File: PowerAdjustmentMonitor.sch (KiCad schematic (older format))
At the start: 0 parts

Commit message: Added power conditioning outline
did not add current sensing circuit
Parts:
- added JP? (x3): JUMPER, ~, symbol JUMPER
- added R? (x6): R, ~, symbol R
- added R? (x2): RVAR, ~, symbol RVAR
- added U? (x2): LM317H, TO-39, symbol LM317H
- added U? (x2): 7805, symbol 7805
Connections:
- new net: R?.1, R?.2, U?.2 (ADJ)
- new net: R?.2, R?.2, U?.2 (ADJ)
- new net +12V: JP?.1, U?.1 (IN), U?.VI
- new net -12V: JP?.2, U?.1 (IN), U?.VI
- new net AGND: JP?.2, R?.1, R?.1, R?.1, R?.2, U?.GND, U?.GND
- new net FE_V+: JP?.2, U?.VO
- new net V+_ADJ: R?.1, R?.1, U?.3 (OUT)
- new net V+_ADJ_MON: R?.1, R?.2
- new net V-: JP?.1, U?.VO
- new net V-_ADJ: R?.2, R?.2, U?.3 (OUT)
- new net V-_ADJ_MON: R?.1, R?.2

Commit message: Added missing bit
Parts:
- added R? (x2): R, ~, symbol R
- added U? (x2): LM324, symbol LM324
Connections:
- net labels added: V+_MON, V-_MON
- wire segments 53 -> 75
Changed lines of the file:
@@
 Sheet 9 9
 Title ""
-Date "3 feb 2014"
+Date "4 feb 2014"
 Rev ""
 Comp ""
@@
 Text HLabel 5500 6700 2    60   Output ~ 0
 V-_ADJ
-Text HLabel 8000 3300 2    60   Output ~ 0
+Text HLabel 8550 1950 2    60   Output ~ 0
 3V3_MON
-Text HLabel 8000 3450 2    60   Output ~ 0
+Text HLabel 8550 2100 2    60   Output ~ 0
 5V_MON
 Text HLabel 6550 2600 2    60   Output ~ 0
@@
 Text HLabel 6550 5200 2    60   Output ~ 0
 V-_ADJ_MON
-Text HLabel 8000 3900 2    60   Output ~ 0
+Text HLabel 8550 2550 2    60   Output ~ 0
 V+_CURR_MON
-Text HLabel 8000 4050 2    60   Output ~ 0
+Text HLabel 8550 2700 2    60   Output ~ 0
 V-_CURR_MON
 $Comp
@@
 Connection ~ 4050 6000
 Wire Wire Line
-	4050 6700 5500 6700
-Wire Wire Line
 	3850 1200 3850 1350
 Wire Wire Line
@@
 	3450 1900 3450 1500
 Connection ~ 3850 1900
-Wire Wire Line
-	3850 1200 5400 1200
 Wire Wire Line
 	3100 1200 3050 1200
@@
 L +3.3V #PWR?
 U 1 1 52F00C77
-P 7800 3100
-F 0 "#PWR?" H 7800 3060 30  0001 C CNN
-F 1 "+3.3V" H 7800 3210 30  0000 C CNN
-F 2 "" H 7800 3100 60  0000 C CNN
-F 3 "" H 7800 3100 60  0000 C CNN
-	1    7800 3100
+P 8350 1750
+F 0 "#PWR?" H 8350 1710 30  0001 C CNN
+F 1 "+3.3V" H 8350 1860 30  0000 C CNN
+F 2 "" H 8350 1750 60  0000 C CNN
+F 3 "" H 8350 1750 60  0000 C CNN
+	1    8350 1750
 	1    0    0    -1
 $EndComp
@@
 L +5V #PWR?
 U 1 1 52F00C86
-P 7550 3100
-F 0 "#PWR?" H 7550 3190 20  0001 C CNN
-F 1 "+5V" H 7550 3190 30  0000 C CNN
-F 2 "" H 7550 3100 60  0000 C CNN
-F 3 "" H 7550 3100 60  0000 C CNN
-	1    7550 3100
-	1    0    0    -1
-$EndComp
-Wire Wire Line
-	7550 3100 7550 3450
-Wire Wire Line
-	7550 3450 8000 3450
-Wire Wire Line
-	7800 3100 7800 3300
-Wire Wire Line
-	7800 3300 8000 3300
+P 8100 1750
+F 0 "#PWR?" H 8100 1840 20  0001 C CNN
+F 1 "+5V" H 8100 1840 30  0000 C CNN
+F 2 "" H 8100 1750 60  0000 C CNN
+F 3 "" H 8100 1750 60  0000 C CNN
+	1    8100 1750
+	1    0    0    -1
+$EndComp
+Wire Wire Line
+	8100 1750 8100 2100
+Wire Wire Line
+	8100 2100 8550 2100
+Wire Wire Line
+	8350 1750 8350 1950
+Wire Wire Line
+	8350 1950 8550 1950
 $Comp
 L RVAR R?
@@
 	1    0    0    -1
 $EndComp
+Wire Wire Line
+	2150 3950 2150 4200
+$Comp
+L R R?
+U 1 1 52F0BD17
+P 4600 6700
+F 0 "R?" V 4680 6700 40  0000 C CNN
+F 1 "R" V 4607 6701 40  0000 C CNN
+F 2 "~" V 4530 6700 30  0000 C CNN
+F 3 "~" H 4600 6700 30  0000 C CNN
+	1    4600 6700
+	0    -1   -1   0
+$EndComp
+Wire Wire Line
+	4050 6700 4350 6700
+Wire Wire Line
+	4850 6700 5500 6700
+Wire Wire Line
+	4250 6700 4250 6050
+Wire Wire Line
+	4250 6050 4900 6050
+Connection ~ 4250 6700
+Text Label 4500 6050 0    60   ~ 0
+V-_MON
+$Comp
+L R R?
+U 1 1 52F0BE4B
+P 4550 1200
+F 0 "R?" V 4630 1200 40  0000 C CNN
+F 1 "R" V 4557 1201 40  0000 C CNN
+F 2 "~" V 4480 1200 30  0000 C CNN
+F 3 "~" H 4550 1200 30  0000 C CNN
+	1    4550 1200
+	0    -1   -1   0
+$EndComp
+Wire Wire Line
+	4800 1200 5400 1200
+Wire Wire Line
+	4300 1200 3850 1200
+Wire Wire Line
+	4100 1200 4100 1750
+Wire Wire Line
+	4100 1750 4750 1750
+Wire Wire Line
+	4750 1750 4750 1700
+Connection ~ 4100 1200
+Text Label 4300 1750 0    60   ~ 0
+V+_MON
+$Comp
+L LM324 U?
+U 1 1 52F0BFD8
+P 8750 4200
+F 0 "U?" H 8800 4400 60  0000 C CNN
+F 1 "LM324" H 8900 4000 50  0000 C CNN
+F 2 "" H 8750 4200 60  0000 C CNN
+F 3 "" H 8750 4200 60  0000 C CNN
+	1    8750 4200
+	1    0    0    -1
+$EndComp
+$Comp
+L +12V #PWR?
+U 1 1 52F0BFF6
+P 8650 3650
+F 0 "#PWR?" H 8650 3600 20  0001 C CNN
+F 1 "+12V" H 8650 3750 30  0000 C CNN
+F 2 "" H 8650 3650 60  0000 C CNN
+F 3 "" H 8650 3650 60  0000 C CNN
+	1    8650 3650
+	1    0    0    -1
+$EndComp
+$Comp
+L -12V #PWR?
+U 1 1 52F0C005
+P 8650 4750
+F 0 "#PWR?" H 8650 4880 20  0001 C CNN
+F 1 "-12V" H 8650 4850 30  0000 C CNN
+F 2 "" H 8650 4750 60  0000 C CNN
+F 3 "" H 8650 4750 60  0000 C CNN
+	1    8650 4750
+	-1   0    0    1
+$EndComp
+Wire Wire Line
+	8250 4300 8000 4300
+Wire Wire Line
+	8000 4300 8000 4950
+Wire Wire Line
+	8000 4950 9250 4950
+Wire Wire Line
+	9250 4950 9250 4200
+Wire Wire Line
+	8650 4600 8650 4750
+Wire Wire Line
+	8650 3800 8650 3650
+Wire Wire Line
+	8250 4100 7650 4100
+Text Label 7700 4100 0    60   ~ 0
+V+_MON
+$Comp
+L LM324 U?
+U 1 1 52F0C1B4
+P 8850 5950
+F 0 "U?" H 8900 6150 60  0000 C CNN
+F 1 "LM324" H 9000 5750 50  0000 C CNN
+F 2 "" H 8850 5950 60  0000 C CNN
+F 3 "" H 8850 5950 60  0000 C CNN
+	1    8850 5950
+	1    0    0    -1
+$EndComp
+$Comp
+L +12V #PWR?
+U 1 1 52F0C1BA
+P 8750 5400
+F 0 "#PWR?" H 8750 5350 20  0001 C CNN
+F 1 "+12V" H 8750 5500 30  0000 C CNN
+F 2 "" H 8750 5400 60  0000 C CNN
+F 3 "" H 8750 5400 60  0000 C CNN
+	1    8750 5400
+	1    0    0    -1
+$EndComp
+$Comp
+L -12V #PWR?
+U 1 1 52F0C1C0
+P 8750 6500
+F 0 "#PWR?" H 8750 6630 20  0001 C CNN
+F 1 "-12V" H 8750 6600 30  0000 C CNN
+F 2 "" H 8750 6500 60  0000 C CNN
+F 3 "" H 8750 6500 60  0000 C CNN
+	1    8750 6500
+	-1   0    0    1
+$EndComp
+Wire Wire Line
+	8350 6050 8100 6050
+Wire Wire Line
+	8100 6050 8100 6700
+Wire Wire Line
+	8100 6700 9350 6700
+Wire Wire Line
+	9350 6700 9350 5950
+Wire Wire Line
+	8750 6350 8750 6500
+Wire Wire Line
+	8750 5550 8750 5400
+Wire Wire Line
+	8350 5850 7750 5850
+Text Label 7800 5850 0    60   ~ 0
+V-_MON
 $EndSCHEMATC

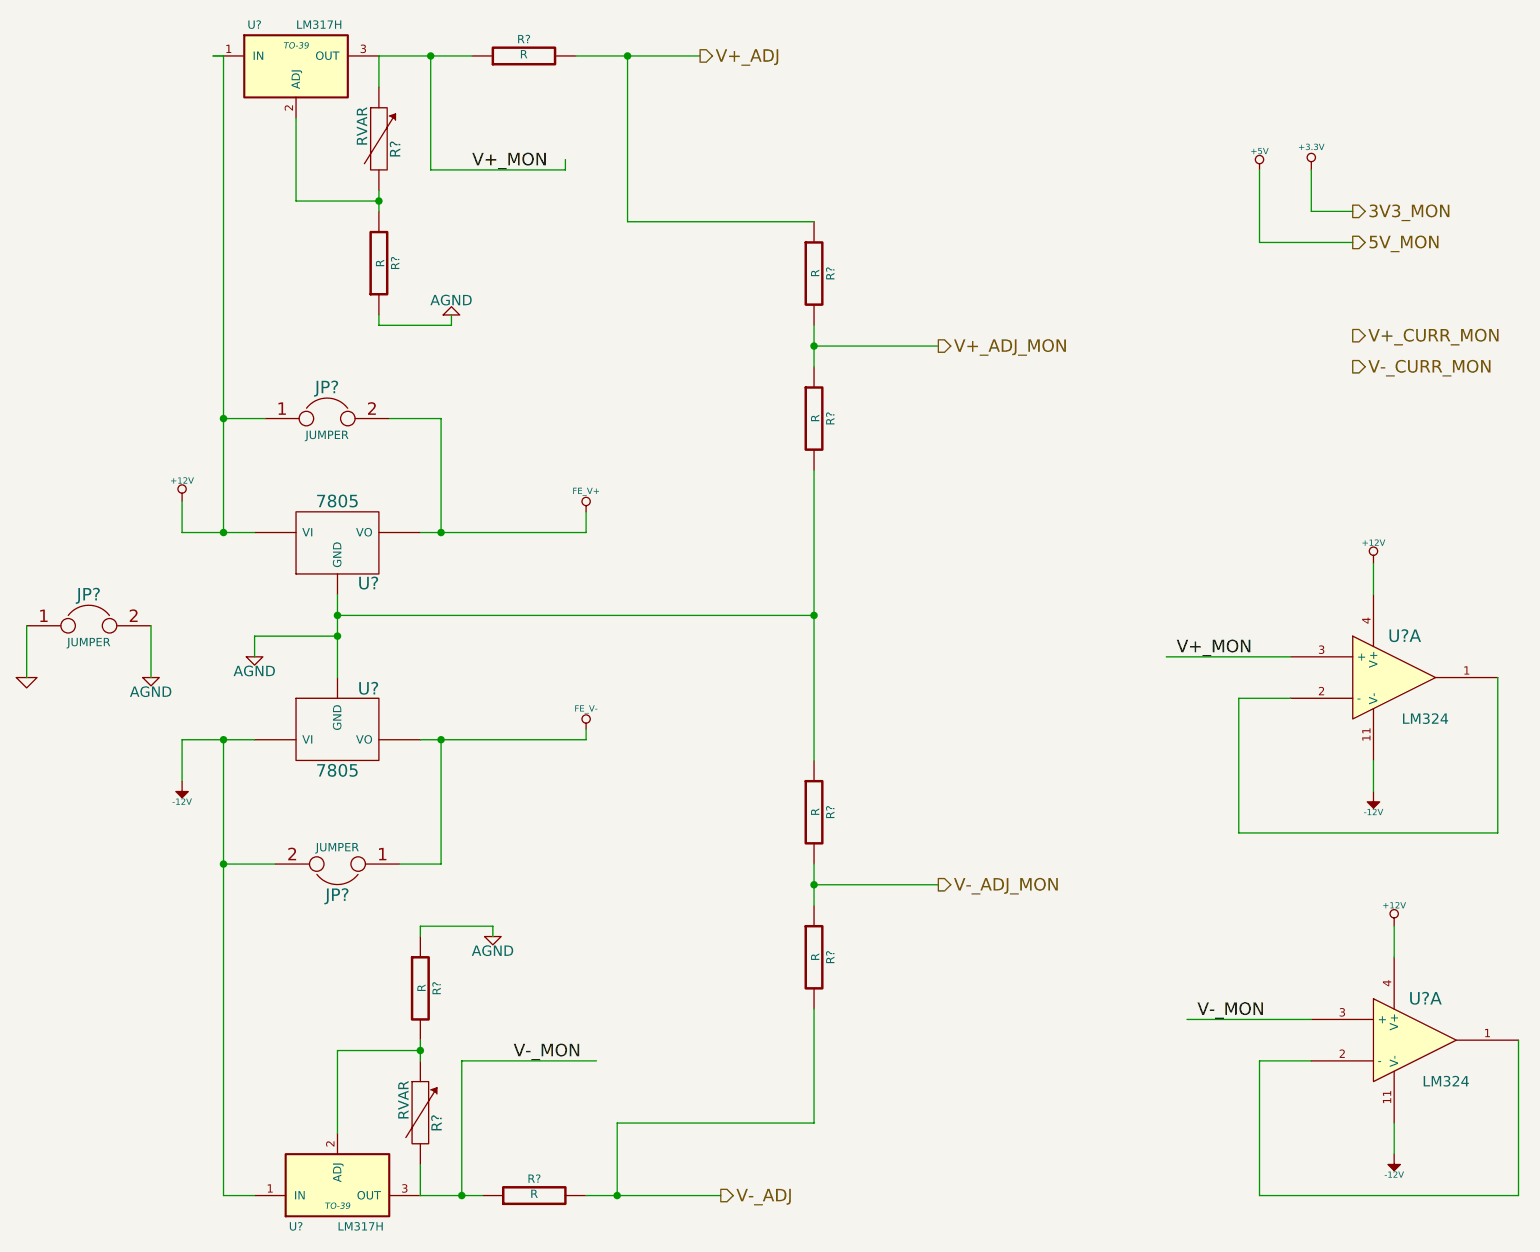
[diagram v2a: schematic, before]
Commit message: Begin Associating relay Module
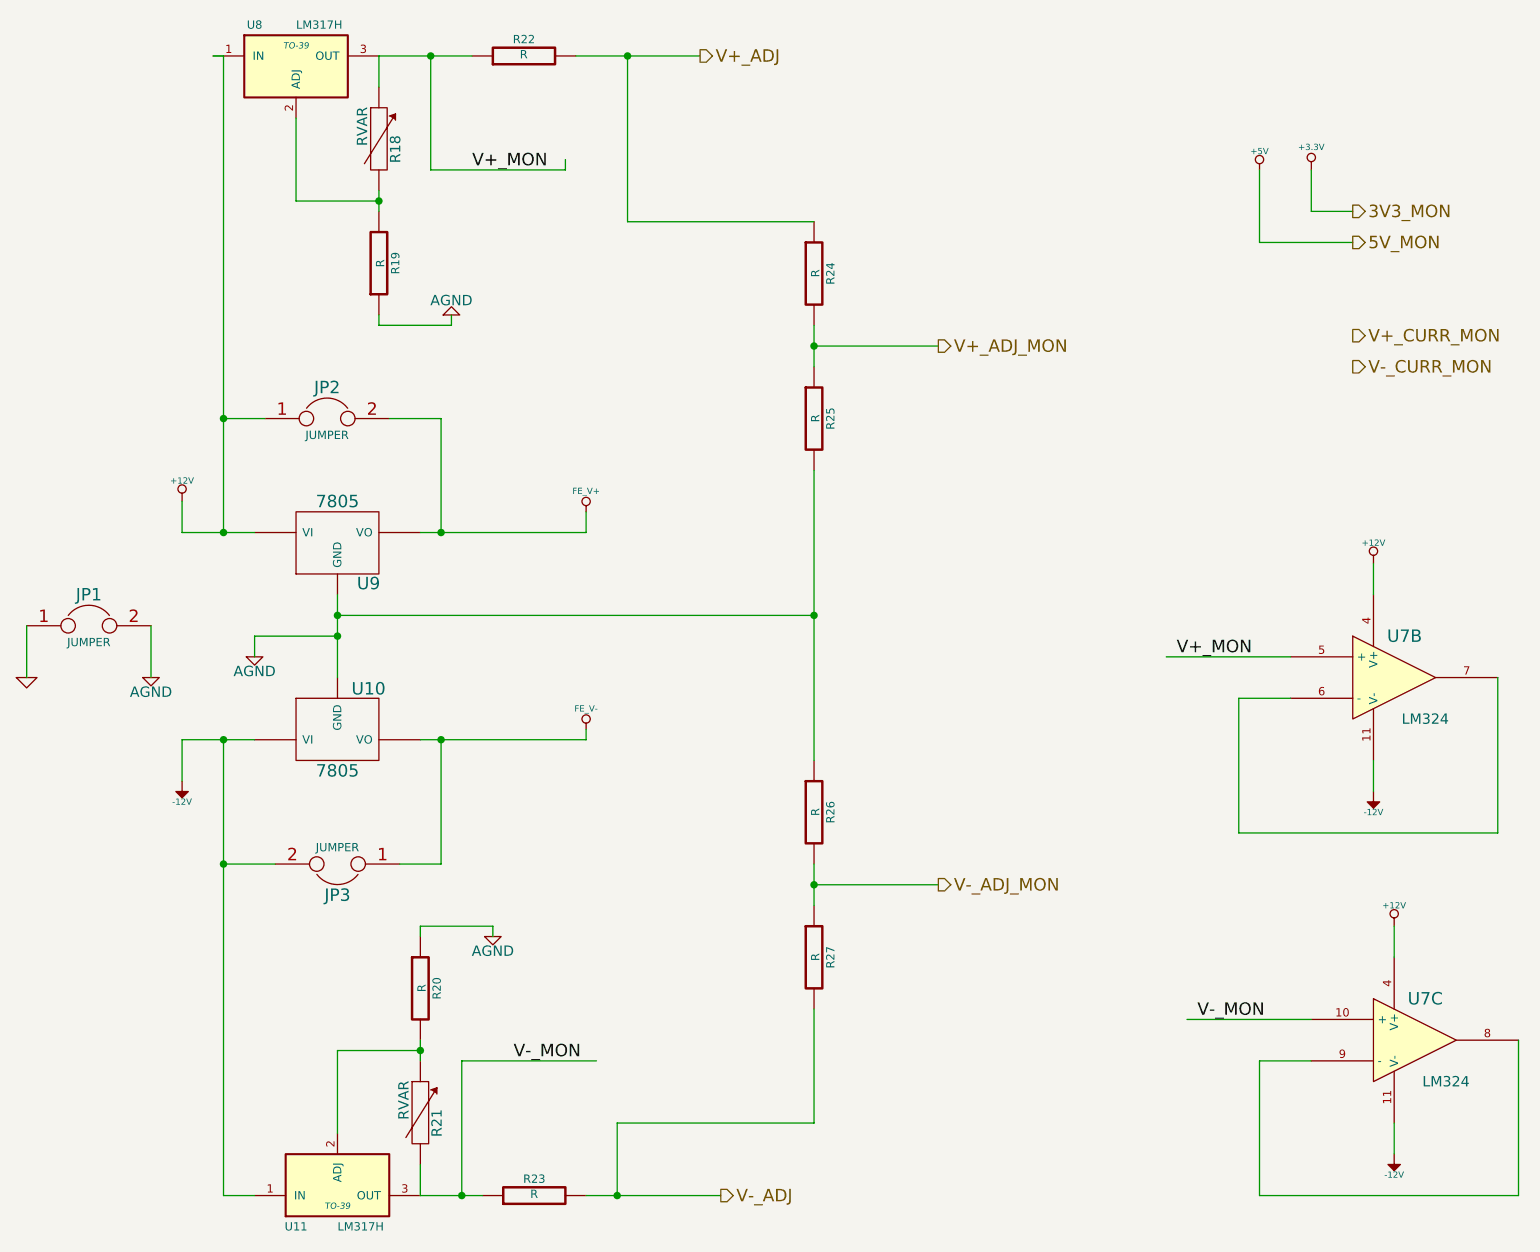
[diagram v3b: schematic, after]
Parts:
- gave numbers to parts that had none: 18
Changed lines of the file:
@@
 LIBS:BenchBudEE
 LIBS:BenchBudEE-cache
-EELAYER 27 0
+EELAYER 24 0
 EELAYER END
 $Descr A4 11693 8268
@@
 $EndDescr
 $Comp
-L +12V #PWR?
+L +12V #PWR41
 U 1 1 52EFE385
 P 2900 3350
-F 0 "#PWR?" H 2900 3300 20  0001 C CNN
+F 0 "#PWR41" H 2900 3300 20  0001 C CNN
 F 1 "+12V" H 2900 3450 30  0000 C CNN
 F 2 "" H 2900 3350 60  0000 C CNN
@@
 $EndComp
 $Comp
-L -12V #PWR?
+L -12V #PWR42
 U 1 1 52EFE394
 P 2900 4700
-F 0 "#PWR?" H 2900 4830 20  0001 C CNN
+F 0 "#PWR42" H 2900 4830 20  0001 C CNN
 F 1 "-12V" H 2900 4800 30  0000 C CNN
 F 2 "" H 2900 4700 60  0000 C CNN
@@
 $EndComp
 $Comp
-L LM317H U?
+L LM317H U11
 U 1 1 52EFE610
 P 3650 6650
-F 0 "U?" H 3450 6850 40  0000 C CNN
+F 0 "U11" H 3450 6850 40  0000 C CNN
 F 1 "LM317H" H 3650 6850 40  0000 L CNN
 F 2 "TO-39" H 3650 6750 30  0000 C CIN
@@
 $EndComp
 $Comp
-L JUMPER JP?
+L JUMPER JP2
 U 1 1 52EFF15A
 P 3600 2950
-F 0 "JP?" H 3600 3100 60  0000 C CNN
+F 0 "JP2" H 3600 3100 60  0000 C CNN
 F 1 "JUMPER" H 3600 2870 40  0000 C CNN
 F 2 "~" H 3600 2950 60  0000 C CNN
@@
 $EndComp
 $Comp
-L JUMPER JP?
+L JUMPER JP3
 U 1 1 52EFF167
 P 3650 5100
-F 0 "JP?" H 3650 5250 60  0000 C CNN
+F 0 "JP3" H 3650 5250 60  0000 C CNN
 F 1 "JUMPER" H 3650 5020 40  0000 C CNN
 F 2 "~" H 3650 5100 60  0000 C CNN
@@
 $EndComp
 $Comp
-L GND #PWR?
+L GND #PWR39
 U 1 1 52EFF203
 P 2150 4200
-F 0 "#PWR?" H 2150 4200 30  0001 C CNN
+F 0 "#PWR39" H 2150 4200 30  0001 C CNN
 F 1 "GND" H 2150 4130 30  0001 C CNN
 F 2 "" H 2150 4200 60  0000 C CNN
@@
 $EndComp
 $Comp
-L AGND #PWR?
+L AGND #PWR40
 U 1 1 52EFF226
 P 2750 4200
-F 0 "#PWR?" H 2750 4200 40  0001 C CNN
+F 0 "#PWR40" H 2750 4200 40  0001 C CNN
 F 1 "AGND" H 2750 4130 50  0000 C CNN
 F 2 "" H 2750 4200 60  0000 C CNN
@@
 $EndComp
 $Comp
-L AGND #PWR?
+L AGND #PWR43
 U 1 1 52EFF247
 P 3250 4100
-F 0 "#PWR?" H 3250 4100 40  0001 C CNN
+F 0 "#PWR43" H 3250 4100 40  0001 C CNN
 F 1 "AGND" H 3250 4030 50  0000 C CNN
 F 2 "" H 3250 4100 60  0000 C CNN
@@
 $EndComp
 $Comp
-L JUMPER JP?
+L JUMPER JP1
 U 1 1 52EFF262
 P 2450 3950
-F 0 "JP?" H 2450 4100 60  0000 C CNN
+F 0 "JP1" H 2450 4100 60  0000 C CNN
 F 1 "JUMPER" H 2450 3870 40  0000 C CNN
 F 2 "~" H 2450 3950 60  0000 C CNN
@@
 $EndComp
 $Comp
-L FE_V+ #PWR?
+L FE_V+ #PWR46
 U 1 1 52EFF50B
 P 4850 3400
-F 0 "#PWR?" H 4850 3500 30  0001 C CNN
+F 0 "#PWR46" H 4850 3500 30  0001 C CNN
 F 1 "FE_V+" H 4850 3500 30  0000 C CNN
 F 2 "" H 4850 3400 60  0000 C CNN
@@
 $EndComp
 $Comp
-L FE_V- #PWR?
+L FE_V- #PWR47
 U 1 1 52EFF51A
 P 4850 4450
-F 0 "#PWR?" H 4850 4550 30  0001 C CNN
+F 0 "#PWR47" H 4850 4550 30  0001 C CNN
 F 1 "FE_V-" H 4850 4550 30  0000 C CNN
 F 2 "" H 4850 4450 60  0000 C CNN
@@
 $EndComp
 $Comp
-L 7805 U?
+L 7805 U9
 U 1 1 52EFF5C9
 P 3650 3550
-F 0 "U?" H 3800 3354 60  0000 C CNN
+F 0 "U9" H 3800 3354 60  0000 C CNN
 F 1 "7805" H 3650 3750 60  0000 C CNN
 F 2 "" H 3650 3550 60  0000 C CNN
@@
 $EndComp
 $Comp
-L 7805 U?
+L 7805 U10
 U 1 1 52EFF5D6
 P 3650 4450
-F 0 "U?" H 3800 4254 60  0000 C CNN
+F 0 "U10" H 3800 4254 60  0000 C CNN
 F 1 "7805" H 3650 4650 60  0000 C CNN
 F 2 "" H 3650 4450 60  0000 C CNN
@@
 $EndComp
 $Comp
-L R R?
+L R R20
 U 1 1 52F006C9
 P 4050 5700
-F 0 "R?" V 4130 5700 40  0000 C CNN
+F 0 "R20" V 4130 5700 40  0000 C CNN
 F 1 "R" V 4057 5701 40  0000 C CNN
 F 2 "~" V 3980 5700 30  0000 C CNN
@@
 $EndComp
 $Comp
-L AGND #PWR?
+L AGND #PWR45
 U 1 1 52F006E7
 P 4400 5450
-F 0 "#PWR?" H 4400 5450 40  0001 C CNN
+F 0 "#PWR45" H 4400 5450 40  0001 C CNN
 F 1 "AGND" H 4400 5380 50  0000 C CNN
 F 2 "" H 4400 5450 60  0000 C CNN
@@
 $EndComp
 $Comp
-L LM317H U?
+L LM317H U8
 U 1 1 52F0077E
 P 3450 1250
-F 0 "U?" H 3250 1450 40  0000 C CNN
+F 0 "U8" H 3250 1450 40  0000 C CNN
 F 1 "LM317H" H 3450 1450 40  0000 L CNN
 F 2 "TO-39" H 3450 1350 30  0000 C CIN
@@
 $EndComp
 $Comp
-L R R?
+L R R19
 U 1 1 52F0078C
 P 3850 2200
-F 0 "R?" V 3930 2200 40  0000 C CNN
+F 0 "R19" V 3930 2200 40  0000 C CNN
 F 1 "R" V 3857 2201 40  0000 C CNN
 F 2 "~" V 3780 2200 30  0000 C CNN
@@
 $EndComp
 $Comp
-L AGND #PWR?
+L AGND #PWR44
 U 1 1 52F00792
 P 4200 2450
-F 0 "#PWR?" H 4200 2450 40  0001 C CNN
+F 0 "#PWR44" H 4200 2450 40  0001 C CNN
 F 1 "AGND" H 4200 2380 50  0000 C CNN
 F 2 "" H 4200 2450 60  0000 C CNN
@@
 V-_CURR_MON
 $Comp
-L R R?
+L R R24
 U 1 1 52F009BA
 P 5950 2250
-F 0 "R?" V 6030 2250 40  0000 C CNN
+F 0 "R24" V 6030 2250 40  0000 C CNN
 F 1 "R" V 5957 2251 40  0000 C CNN
 F 2 "~" V 5880 2250 30  0000 C CNN
@@
 $EndComp
 $Comp
-L R R?
+L R R25
 U 1 1 52F009C7
 P 5950 2950
-F 0 "R?" V 6030 2950 40  0000 C CNN
+F 0 "R25" V 6030 2950 40  0000 C CNN
 F 1 "R" V 5957 2951 40  0000 C CNN
 F 2 "~" V 5880 2950 30  0000 C CNN
@@
 Connection ~ 3650 3900
 $Comp
-L R R?
+L R R26
 U 1 1 52F00AFF
 P 5950 4850
-F 0 "R?" V 6030 4850 40  0000 C CNN
+F 0 "R26" V 6030 4850 40  0000 C CNN
 F 1 "R" V 5957 4851 40  0000 C CNN
 F 2 "~" V 5880 4850 30  0000 C CNN
@@
 $EndComp
 $Comp
-L R R?
+L R R27
 U 1 1 52F00B05
 P 5950 5550
-F 0 "R?" V 6030 5550 40  0000 C CNN
+F 0 "R27" V 6030 5550 40  0000 C CNN
 F 1 "R" V 5957 5551 40  0000 C CNN
 F 2 "~" V 5880 5550 30  0000 C CNN
@@
 Connection ~ 5950 2600
 $Comp
-L +3.3V #PWR?
+L +3.3V #PWR49
 U 1 1 52F00C77
 P 8350 1750
-F 0 "#PWR?" H 8350 1710 30  0001 C CNN
+F 0 "#PWR49" H 8350 1710 30  0001 C CNN
 F 1 "+3.3V" H 8350 1860 30  0000 C CNN
 F 2 "" H 8350 1750 60  0000 C CNN
@@
 $EndComp
 $Comp
-L +5V #PWR?
+L +5V #PWR48
 U 1 1 52F00C86
 P 8100 1750
-F 0 "#PWR?" H 8100 1840 20  0001 C CNN
+F 0 "#PWR48" H 8100 1840 20  0001 C CNN
 F 1 "+5V" H 8100 1840 30  0000 C CNN
 F 2 "" H 8100 1750 60  0000 C CNN
@@
 	8350 1950 8550 1950
 $Comp
-L RVAR R?
+L RVAR R18
 U 1 1 52F00D47
 P 3850 1600
-F 0 "R?" V 3930 1550 50  0000 C CNN
+F 0 "R18" V 3930 1550 50  0000 C CNN
 F 1 "RVAR" V 3770 1660 50  0000 C CNN
 F 2 "~" H 3850 1600 60  0000 C CNN
@@
 $EndComp
 $Comp
-L RVAR R?
+L RVAR R21
 U 1 1 52F00D54
 P 4050 6300
-F 0 "R?" V 4130 6250 50  0000 C CNN
+F 0 "R21" V 4130 6250 50  0000 C CNN
 F 1 "RVAR" V 3970 6360 50  0000 C CNN
 F 2 "~" H 4050 6300 60  0000 C CNN
@@
 	2150 3950 2150 4200
 $Comp
-L R R?
+L R R23
 U 1 1 52F0BD17
 P 4600 6700
-F 0 "R?" V 4680 6700 40  0000 C CNN
+F 0 "R23" V 4680 6700 40  0000 C CNN
 F 1 "R" V 4607 6701 40  0000 C CNN
 F 2 "~" V 4530 6700 30  0000 C CNN
@@
 V-_MON
 $Comp
-L R R?
+L R R22
 U 1 1 52F0BE4B
 P 4550 1200
-F 0 "R?" V 4630 1200 40  0000 C CNN
+F 0 "R22" V 4630 1200 40  0000 C CNN
 F 1 "R" V 4557 1201 40  0000 C CNN
 F 2 "~" V 4480 1200 30  0000 C CNN
@@
 V+_MON
 $Comp
-L LM324 U?
-U 1 1 52F0BFD8
+L LM324 U7
+U 2 1 52F0BFD8
 P 8750 4200
-F 0 "U?" H 8800 4400 60  0000 C CNN
+F 0 "U7" H 8800 4400 60  0000 C CNN
 F 1 "LM324" H 8900 4000 50  0000 C CNN
 F 2 "" H 8750 4200 60  0000 C CNN
 F 3 "" H 8750 4200 60  0000 C CNN
-	1    8750 4200
-	1    0    0    -1
-$EndComp
-$Comp
-L +12V #PWR?
+	2    8750 4200
+	1    0    0    -1
+$EndComp
+$Comp
+L +12V #PWR50
 U 1 1 52F0BFF6
 P 8650 3650
-F 0 "#PWR?" H 8650 3600 20  0001 C CNN
+F 0 "#PWR50" H 8650 3600 20  0001 C CNN
 F 1 "+12V" H 8650 3750 30  0000 C CNN
 F 2 "" H 8650 3650 60  0000 C CNN
@@
 $EndComp
 $Comp
-L -12V #PWR?
+L -12V #PWR51
 U 1 1 52F0C005
 P 8650 4750
-F 0 "#PWR?" H 8650 4880 20  0001 C CNN
+F 0 "#PWR51" H 8650 4880 20  0001 C CNN
 F 1 "-12V" H 8650 4850 30  0000 C CNN
 F 2 "" H 8650 4750 60  0000 C CNN
@@
 V+_MON
 $Comp
-L LM324 U?
-U 1 1 52F0C1B4
+L LM324 U7
+U 3 1 52F0C1B4
 P 8850 5950
-F 0 "U?" H 8900 6150 60  0000 C CNN
+F 0 "U7" H 8900 6150 60  0000 C CNN
 F 1 "LM324" H 9000 5750 50  0000 C CNN
 F 2 "" H 8850 5950 60  0000 C CNN
 F 3 "" H 8850 5950 60  0000 C CNN
-	1    8850 5950
-	1    0    0    -1
-$EndComp
-$Comp
-L +12V #PWR?
+	3    8850 5950
+	1    0    0    -1
+$EndComp
+$Comp
+L +12V #PWR52
 U 1 1 52F0C1BA
 P 8750 5400
-F 0 "#PWR?" H 8750 5350 20  0001 C CNN
+F 0 "#PWR52" H 8750 5350 20  0001 C CNN
 F 1 "+12V" H 8750 5500 30  0000 C CNN
 F 2 "" H 8750 5400 60  0000 C CNN
@@
 $EndComp
 $Comp
-L -12V #PWR?
+L -12V #PWR53
 U 1 1 52F0C1C0
 P 8750 6500
-F 0 "#PWR?" H 8750 6630 20  0001 C CNN
+F 0 "#PWR53" H 8750 6630 20  0001 C CNN
 F 1 "-12V" H 8750 6600 30  0000 C CNN
 F 2 "" H 8750 6500 60  0000 C CNN
